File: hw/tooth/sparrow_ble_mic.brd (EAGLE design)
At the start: 10.5 x 10.5 mm, 25 parts, among them Q2 FA-128

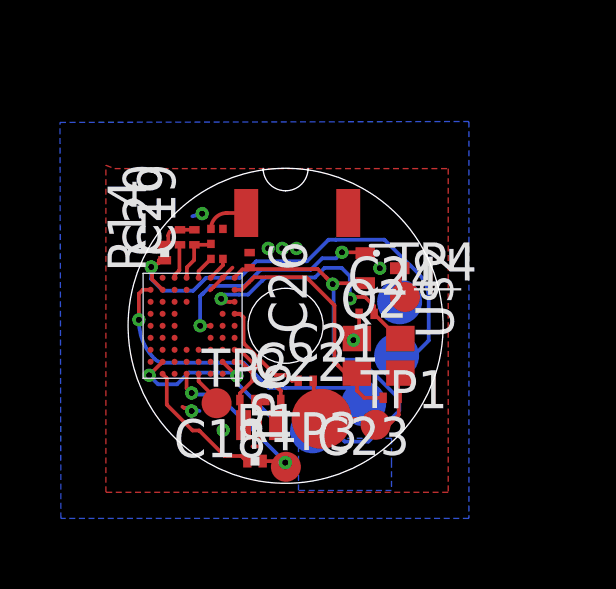
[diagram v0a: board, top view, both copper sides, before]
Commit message: hw: Update tooth design for nRF52832
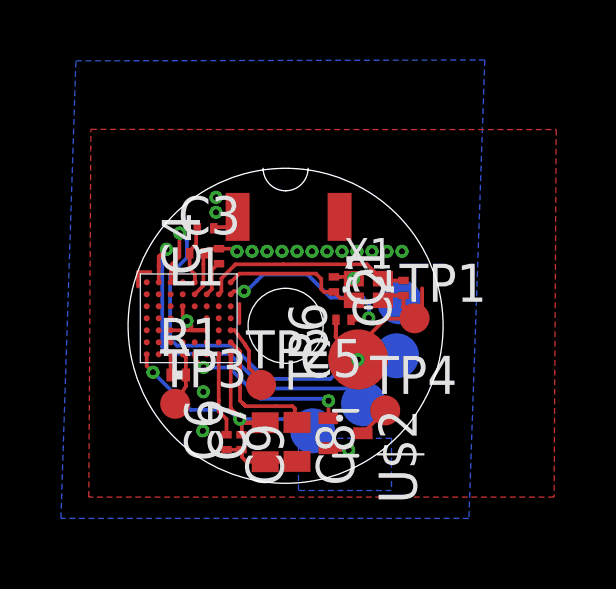
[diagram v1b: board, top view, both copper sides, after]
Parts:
- removed C18, C22, C23, C24: (no value), rcl:C0201
- removed C19: 2.2nF, rcl:C0201
- removed C20, C21: 47nF, rcl:C0201
- removed C26: 1nF, rcl:C0201
- removed IC1: (no value), dan:2450BM08B0003T
- removed IC3: (no value), dan:WLCSP-CDAB62
- removed Q2: FA-128, smartwatch:FA-128
- removed R14: 12K, rcl:R0201
- removed U$1: 2450AT18A100, dan:2450AT18A100
- removed U$4: ABS05, dan:ABS05
- added C1, C2: 12pF, rcl:C0201
- added C3: 1pF, rcl:C0201
- added C4, C5: 100pF, rcl:C0201
- added C6, C9: 100nF, rcl:C0201
- added C7: 4.7uF, rcl:C0402
- added C8: 1uF, rcl:C0402
- added IC2: (no value), dan:NRF52832_WLCSP
- added L1: 3.3nH, rcl:L0201
- added U$3: 2450AT18A100, dan:2450AT18A100
- added X1: 416F32022CKR, crystals:M416
- moved U$2 5.64 mm to (2.00, -3.58)
- moved TP3 4.25 mm to (-3.68, -2.60)
- moved R1 3.85 mm to (-3.58, -1.64)
- moved TP4 3.84 mm to (3.32, -2.82)
- moved TP1 3.78 mm to (4.30, 0.25)
- moved TP6 2.33 mm to (2.42, -1.12)
- moved TP2 1.60 mm to (-0.82, -1.97)
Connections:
- removed net AREF: IC3.C9
- removed net N$11: C21.1, IC3.A4
- removed net N$15: C20.1, IC3.F1
- removed net N$16: C19.1, IC1.2, IC3.E1
- removed net N$17: C24.2, IC3.A3, Q2.3
- removed net N$18: C23.2, IC3.A2, Q2.1
- removed net N$3: IC1.3, IC3.D1
- removed net N$4: IC1.1, U$1.P$1
- removed net N$7: C18.2, IC3.A8, U$4.P$1
- removed net N$8: C22.2, IC3.A7, U$4.P$2
- new net AIN0: IC2.C6
- new net AIN1: IC2.D6
- new net AIN6: IC2.A5, TP2.TP
- new net AIN7: IC2.B5
- new net N$10: C5.1, IC2.A2
- new net N$12: C3.1, IC2.D1, L1.2
- new net N$13: L1.1, U$3.P$1
- new net N$19: C9.1, IC2.B7
- new net N$2: C2.2, IC2.A1, X1.1
- new net N$20: C8.1, IC2.A6
- new net N$6: C1.2, IC2.B2, X1.3
- new net N$9: C4.1, IC2.C2
- net 3.3V: now also C6.2, C7.2, IC2.A7, IC2.H7; no longer C26.2, IC3.A1, IC3.B8, IC3.G8
- net AIN2: now also IC2.E6; no longer IC3.E7
- net AIN3: now also IC2.E7, R1.2, TP3.TP; no longer IC3.D9, TP2.TP
- net AIN4: now also IC2.A3; no longer IC3.E9, R1.2, TP3.TP
- net AIN5: now also IC2.A4; no longer IC3.E8
- net GND: now also C1.1, C2.1, C3.2, C4.2, C5.2, C6.1, C7.1, C8.2, C9.2, IC2.C4, IC2.C5, IC2.D2, IC2.E3, IC2.F5, X1.2, X1.4; no longer C18.1, C19.2, C20.2, C21.2, C22.1, C23.1, C24.1, C26.1, IC1.5, IC3.B1, IC3.B4, IC3.D7, IC3.F4, IC3.F6, IC3.F9, Q2.2, Q2.4, R14.2
- net HON: now also IC2.F7; no longer IC3.G9
- net N$1: now also IC2.H1; no longer IC1.4, IC3.C1
- net SON: now also IC2.D7; no longer IC3.C5
- net SWDCLK: now also IC2.F1; no longer IC3.G2, R14.1
- net SWDIO: now also IC2.G1; no longer IC3.H2
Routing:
- net N$17: track 8.53 -> 0.00 mm, vias 2 -> 0
- net N$18: track 8.23 -> 0.00 mm
- net 3.3V: track 22.2 -> 14.6 mm
- net N$6: track 0.00 -> 7.03 mm
- net N$10: track 0.00 -> 6.45 mm, vias 0 -> 2
- net AIN4: track 6.09 -> 0.00 mm, vias 2 -> 0
- net GND: track 13.8 -> 19.1 mm, vias 8 -> 19
- net N$2: track 0.00 -> 4.79 mm
- net N$20: track 0.00 -> 4.52 mm
- net HON: track 4.69 -> 0.69 mm
- net N$11: track 3.88 -> 0.00 mm
- net N$8: track 3.55 -> 0.00 mm
- net N$19: track 0.00 -> 3.07 mm
- net AIN6: track 0.00 -> 2.27 mm
- net N$7: track 2.79 -> 0.65 mm
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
